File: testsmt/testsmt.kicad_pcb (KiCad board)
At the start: 2 copper layers, 100 x 100 mm, 47 parts, among them J1 DIN-5_180degree, J2 Conn_01x16, J3 Conn_01x16, J4 Conn_01x16, J5 AudioJack3_Ground_Switch, U1 6N138, U2 Teensy3.2, U3 4051, U4 4051, U5 4051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

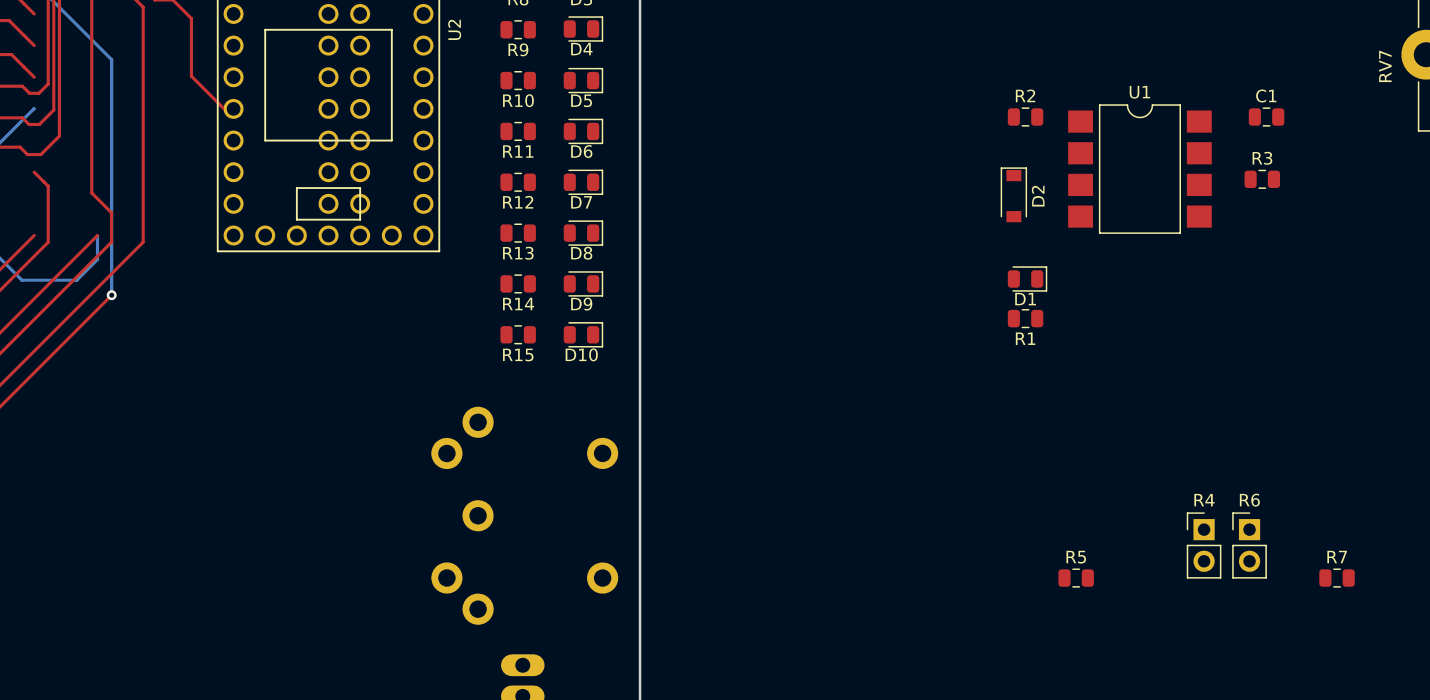
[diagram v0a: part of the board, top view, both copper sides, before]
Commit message: fsr in place
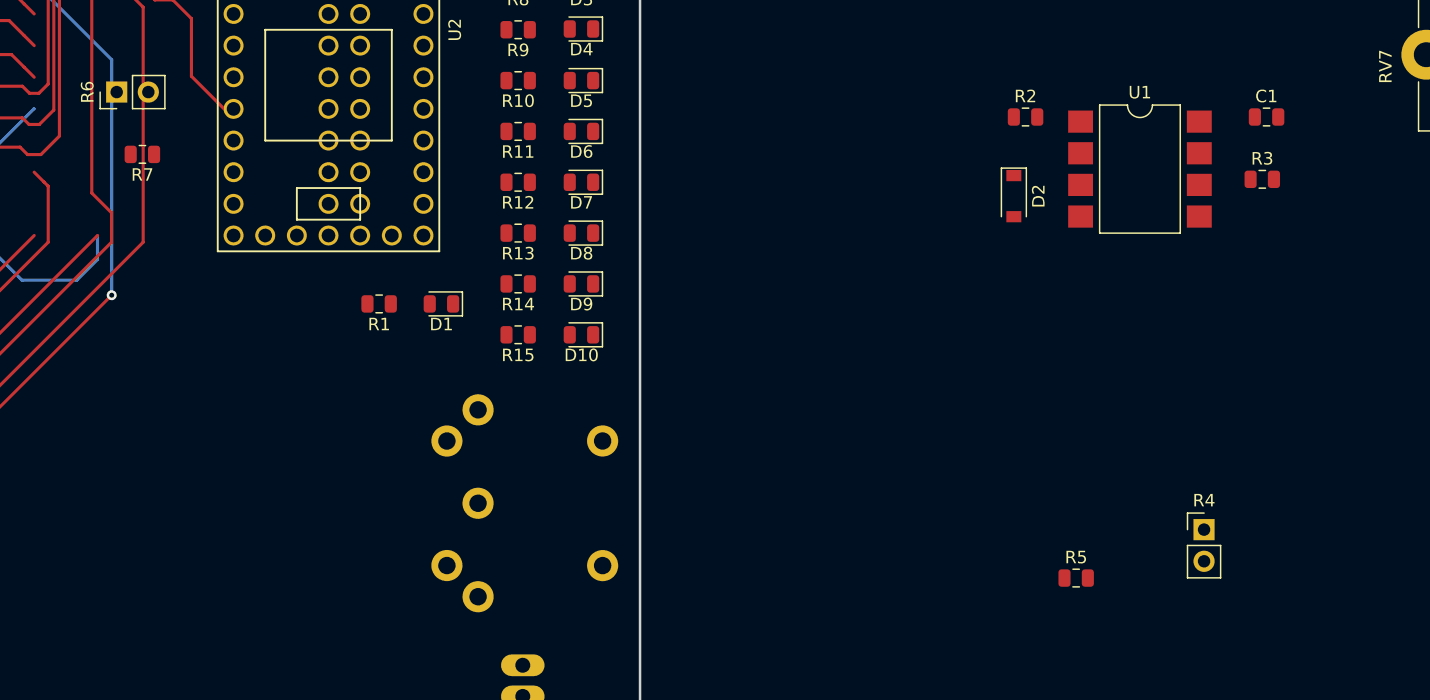
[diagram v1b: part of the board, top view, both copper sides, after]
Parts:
- moved R7 101.7 mm to (105.1, 56.0), turned to 180 degrees
- moved R6 97.5 mm to (103.0, 51.0), turned to 90 degrees
- moved R1 51.9 mm to (124.1, 68.0)
- moved D1 46.9 mm to (129.1, 68.0)
- moved J1 1.00 mm to (135.0, 84.0)
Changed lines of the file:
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@@
   (general
     (thickness 1.6)
-    (drawings 9)
+    (drawings 19)
     (tracks 465)
     (zones 0)
@@
   )
   (module Connector_PinHeader_2.54mm:PinHeader_1x02_P2.54mm_Vertical (layer F.Cu)
-    (at 193.915001 86.115001)
+    (at 103 51 90)
     (descr "Through hole straight pin header, 1x02, 2.54mm pitch, single row")
     (tags "Through hole pin header THT 1x02 2.54mm single row")
-    (fp_text reference R6 (at 0 -2.33) (layer F.SilkS)
-      (effects (font (size 1 1) (thickness 0.15)))
-    )
-    (fp_text value R_FORCE (at 0 4.87) (layer F.Fab)
-      (effects (font (size 1 1) (thickness 0.15)))
-    )
-    (fp_text user %R (at 0 1.27 90) (layer F.Fab)
+    (fp_text reference R6 (at 0 -2.33 90) (layer F.SilkS)
+      (effects (font (size 1 1) (thickness 0.15)))
+    )
+    (fp_text value R_FORCE (at 0 4.87 90) (layer F.Fab)
+      (effects (font (size 1 1) (thickness 0.15)))
+    )
+    (fp_text user %R (at 0 1.27 180) (layer F.Fab)
       (effects (font (size 1 1) (thickness 0.15)))
     )
@@
     (fp_line (start 1.27 -1.27) (end 1.27 3.81) (layer F.Fab) (width 0.1))
     (fp_line (start -0.635 -1.27) (end 1.27 -1.27) (layer F.Fab) (width 0.1))
-    (pad 2 thru_hole oval (at 0 2.54) (size 1.7 1.7) (drill 1) (layers *.Cu *.Mask)
+    (pad 2 thru_hole oval (at 0 2.54 90) (size 1.7 1.7) (drill 1) (layers *.Cu *.Mask)
       (net 66 /FSR))
-    (pad 1 thru_hole rect (at 0 0) (size 1.7 1.7) (drill 1) (layers *.Cu *.Mask)
+    (pad 1 thru_hole rect (at 0 0 90) (size 1.7 1.7) (drill 1) (layers *.Cu *.Mask)
       (net 5 +3V3))
     (model ${KISYS3DMOD}/Connector_PinHeader_2.54mm.3dshapes/PinHeader_1x02_P2.54mm_Vertical.wrl
@@
   )
   (module LED_SMD:LED_0805_2012Metric (layer F.Cu)
-    (at 175.9375 66 180)
+    (at 129.0625 68 180)
     (descr "LED SMD 0805 (2012 Metric), square (rectangular) end terminal, IPC_7351 nominal, (Body size source: https://docs.google.com/spreadsheets/d/1BsfQQcO9C6DZCsRaXUlFlo91Tg2WpOkGARC1WS5S8t0/edit?usp=sharing), generated with kicad-footprint-generator")
     (tags diode)
@@
   )
   (module Resistor_SMD:R_0805_2012Metric (layer F.Cu)
-    (at 200.9375 90)
+    (at 105.0625 56 180)
     (descr "Resistor SMD 0805 (2012 Metric), square (rectangular) end terminal, IPC_7351 nominal, (Body size source: https://docs.google.com/spreadsheets/d/1BsfQQcO9C6DZCsRaXUlFlo91Tg2WpOkGARC1WS5S8t0/edit?usp=sharing), generated with kicad-footprint-generator")
     (tags resistor)
     (attr smd)
-    (fp_text reference R7 (at 0 -1.65) (layer F.SilkS)
-      (effects (font (size 1 1) (thickness 0.15)))
-    )
-    (fp_text value 10K (at 0 1.65) (layer F.Fab)
+    (fp_text reference R7 (at 0 -1.65 180) (layer F.SilkS)
+      (effects (font (size 1 1) (thickness 0.15)))
+    )
+    (fp_text value 10K (at 0 1.65 180) (layer F.Fab)
       (effects (font (size 1 1) (thickness 0.15)))
     )
@@
     (fp_line (start 1.68 -0.95) (end 1.68 0.95) (layer F.CrtYd) (width 0.05))
     (fp_line (start 1.68 0.95) (end -1.68 0.95) (layer F.CrtYd) (width 0.05))
-    (fp_text user %R (at 0 0) (layer F.Fab)
+    (fp_text user %R (at 0 0 180) (layer F.Fab)
       (effects (font (size 0.5 0.5) (thickness 0.08)))
     )
-    (pad 1 smd roundrect (at -0.9375 0) (size 0.975 1.4) (layers F.Cu F.Paste F.Mask) (roundrect_rratio 0.25)
+    (pad 1 smd roundrect (at -0.9375 0 180) (size 0.975 1.4) (layers F.Cu F.Paste F.Mask) (roundrect_rratio 0.25)
       (net 66 /FSR))
-    (pad 2 smd roundrect (at 0.9375 0) (size 0.975 1.4) (layers F.Cu F.Paste F.Mask) (roundrect_rratio 0.25)
+    (pad 2 smd roundrect (at 0.9375 0 180) (size 0.975 1.4) (layers F.Cu F.Paste F.Mask) (roundrect_rratio 0.25)
       (net 1 GND))
     (model ${KISYS3DMOD}/Resistor_SMD.3dshapes/R_0805_2012Metric.wrl
@@
   )
   (module Resistor_SMD:R_0805_2012Metric (layer F.Cu)
-    (at 175.9375 69.18 180)
+    (at 124.0625 68 180)
     (descr "Resistor SMD 0805 (2012 Metric), square (rectangular) end terminal, IPC_7351 nominal, (Body size source: https://docs.google.com/spreadsheets/d/1BsfQQcO9C6DZCsRaXUlFlo91Tg2WpOkGARC1WS5S8t0/edit?usp=sharing), generated with kicad-footprint-generator")
     (tags resistor)
@@
   )
   (module polymodsmt:MIDI_DIN5 (layer F.Cu)
-    (at 135 85 90)
+    (at 135 84 90)
     (descr "Din 5 (MIDI), Pro Signal P/N PSG03463")
     (fp_text reference J1 (at 0 11.00074 90) (layer F.Fab)
@@
       (net 50 "Net-(U2-Pad52)"))
   )
+  (gr_line (start 99 50) (end 99 92) (layer Dwgs.User) (width 0.2))
+  (gr_line (start 109 50) (end 99 50) (layer Dwgs.User) (width 0.2))
+  (gr_line (start 109 92) (end 109 50) (layer Dwgs.User) (width 0.2))
+  (gr_line (start 99 92) (end 109 92) (layer Dwgs.User) (width 0.2))
+  (gr_circle (center 104 82) (end 114 82) (layer Dwgs.User) (width 0.2))
+  (gr_circle (center 104 82) (end 116 82) (layer Dwgs.User) (width 0.2))
+  (gr_line (start 241 125) (end 221 125) (layer Dwgs.User) (width 0.2))
+  (gr_line (start 241 65) (end 241 125) (layer Dwgs.User) (width 0.2))
+  (gr_line (start 221 65) (end 241 65) (layer Dwgs.User) (width 0.2))
+  (gr_line (start 221 125) (end 221 65) (layer Dwgs.User) (width 0.2))
   (gr_line (start 100 64) (end 100 28) (layer Dwgs.User) (width 0.2))
   (gr_line (start 136 64) (end 100 64) (layer Dwgs.User) (width 0.2))

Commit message: pretty happy with layout
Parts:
- moved RV7 166.2 mm to (55.0, 100.0)
- moved C2 155.5 mm to (63.0, 98.7)
- moved U7 137.7 mm to (79.0, 98.0)
- moved R4 110.3 mm to (80.0, 84.0), turned to 270 degrees
- moved R5 108.1 mm to (72.0, 95.0), turned to 270 degrees
- moved U1 83.9 mm to (113.0, 100.0)
- moved C1 83.9 mm to (123.3, 96.0)
- moved R2 83.9 mm to (103.9, 96.0)
- moved R3 83.9 mm to (122.9, 101.0)
- moved D2 83.9 mm to (103.0, 102.3)
- moved R7 55.1 mm to (72.0, 100.1), turned to 270 degrees
- moved J5 2.24 mm to (141.0, 101.0)
- moved RV1 2.00 mm to (55.0, 121.0)
- moved RV2 2.00 mm to (72.0, 121.0)
- moved RV3 2.00 mm to (89.0, 121.0)
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
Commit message: routing routing routing
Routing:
- net /ADDRESS_READ_B: track 80.3 -> 199.1 mm, vias 0 -> 1
- net /ADDRESS_READ_C: track 74.4 -> 189.4 mm, vias 0 -> 1
- net +3V3: track 174.9 -> 257.6 mm
- net /ADDRESS_READ_A: track 84.5 -> 160.9 mm, vias 0 -> 2
- net /FSR: track 0.00 -> 67.4 mm, vias 0 -> 1
- net /ADDRESS_SEND_C: track 130.2 -> 189.1 mm, vias 1 -> 2
- net /ADDRESS_SEND_B: track 144.4 -> 183.2 mm, vias 1 -> 0
- net /ADDRESS_SEND_A: track 149.6 -> 180.9 mm
- net /CONNECTION_READ_A: track 80.1 -> 102.3 mm
- net /CONNECTION_SEND_A: track 76.4 -> 92.6 mm
- net /CONNECTION_SEND_B: track 57.6 -> 73.7 mm
- net /CONNECTION_READ_B: track 70.9 -> 82.6 mm
- net GND: track 0.00 -> 5.02 mm, vias 0 -> 3

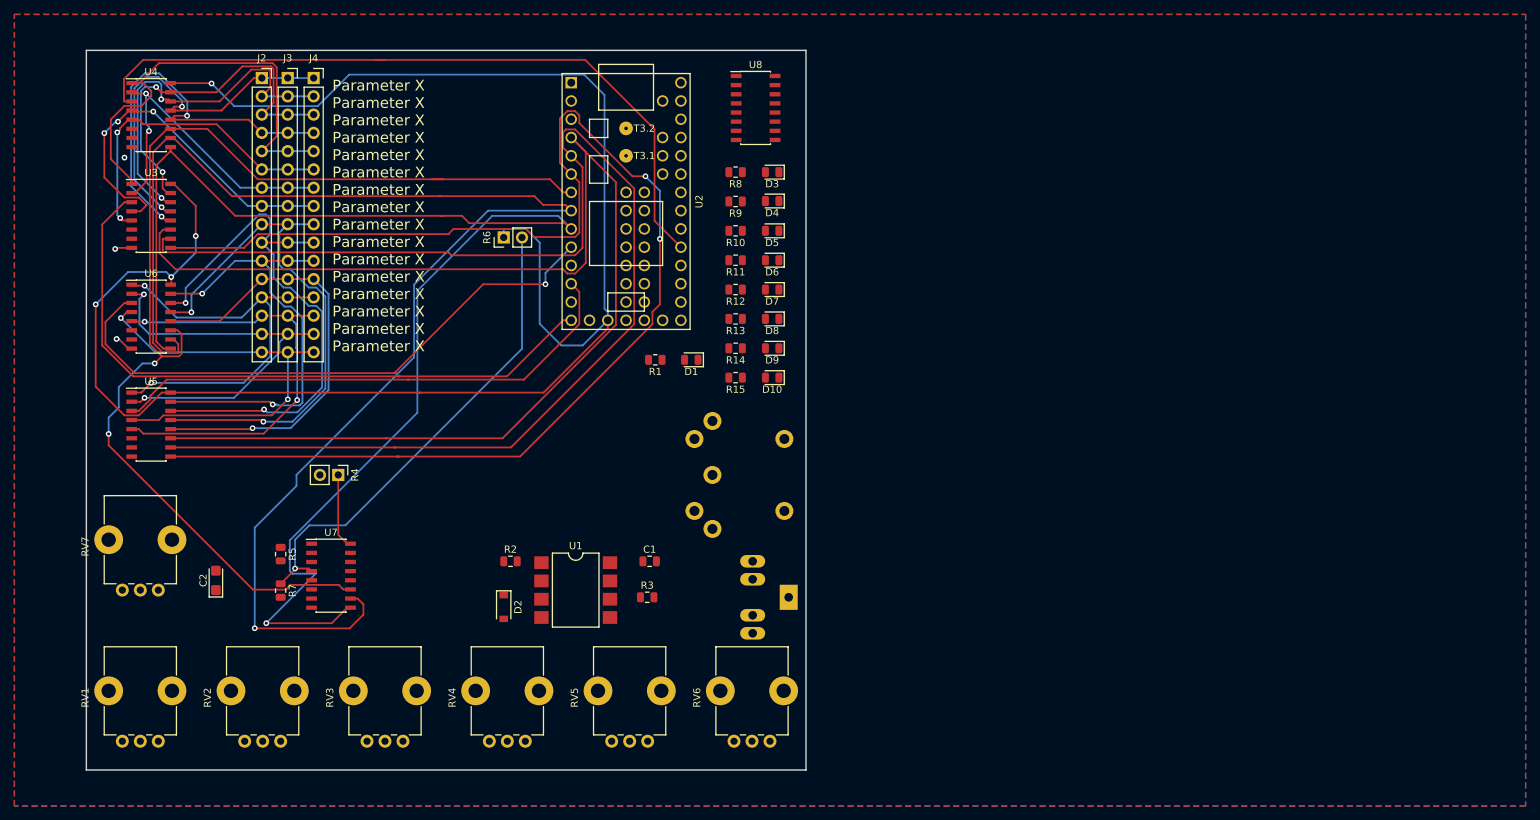
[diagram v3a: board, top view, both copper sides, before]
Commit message: 13 unrouted left
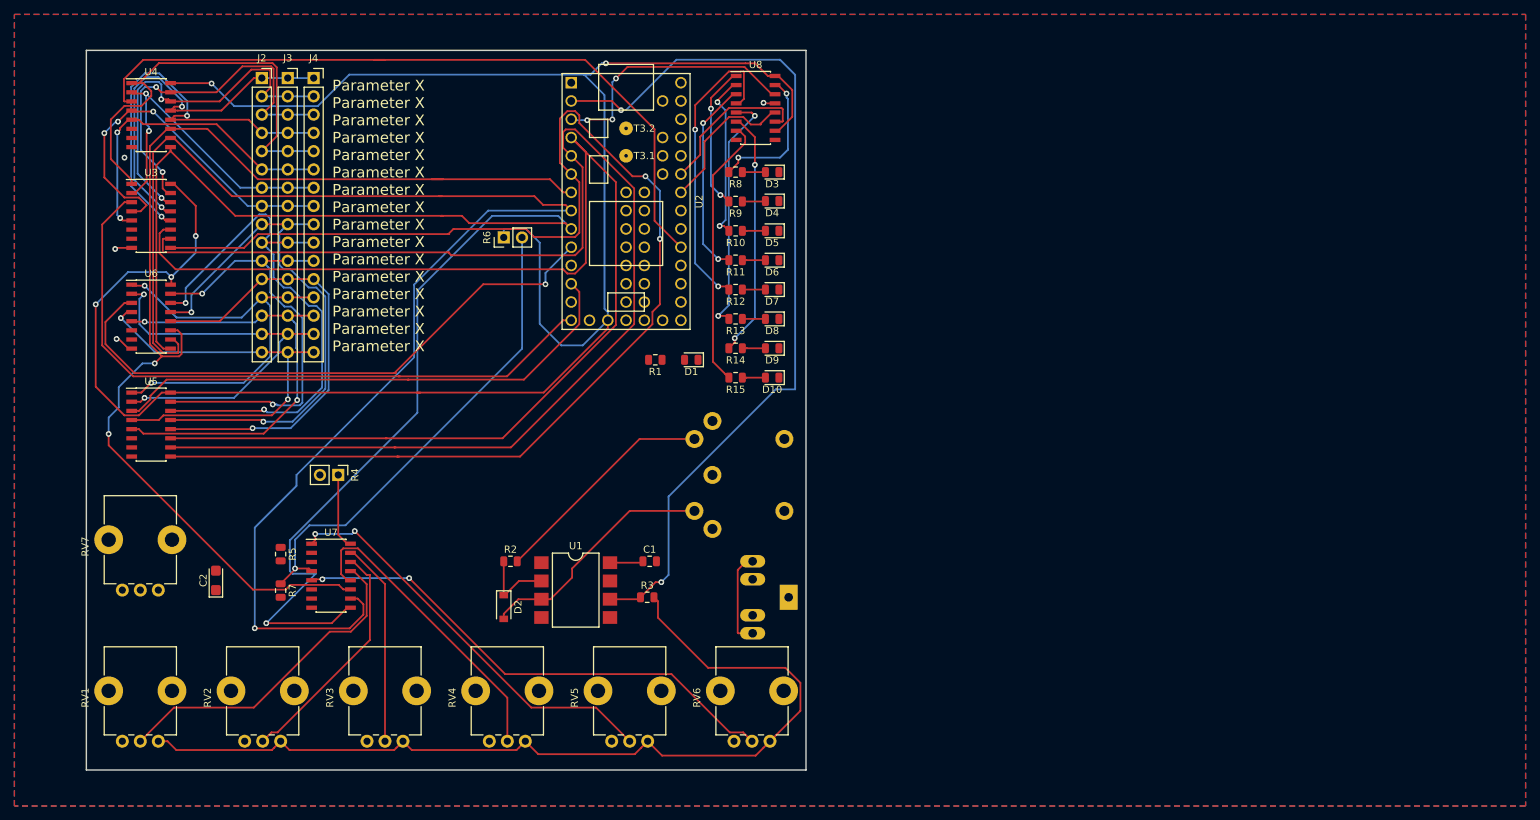
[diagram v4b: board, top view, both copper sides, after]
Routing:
- net +3V3: track 257.6 -> 423.3 mm, vias 4 -> 5
- net /SERIAL_RX: track 0.00 -> 123.3 mm, vias 0 -> 2
- net /KNOB_6: track 0.00 -> 70.7 mm, vias 0 -> 2
- net /KNOB_5: track 0.00 -> 57.5 mm, vias 0 -> 2
- net /KNOB_1: track 0.00 -> 46.1 mm
- net /KNOB_4: track 0.00 -> 42.8 mm
- net Net-(R12-Pad2): track 0.00 -> 42.0 mm, vias 0 -> 2
- net Net-(R15-Pad2): track 0.00 -> 37.9 mm
- net /SHIFT_REG_DATA: track 0.00 -> 36.1 mm, vias 0 -> 3
- net Net-(R13-Pad2): track 0.00 -> 34.4 mm, vias 0 -> 2
- net Net-(R14-Pad2): track 0.00 -> 34.3 mm, vias 0 -> 2
- net Net-(D2-Pad2): track 0.00 -> 33.9 mm
- net /KNOB_2: track 0.00 -> 33.2 mm
- net Net-(J1-Pad4): track 0.00 -> 31.7 mm
- net /KNOB_3: track 0.00 -> 28.4 mm
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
